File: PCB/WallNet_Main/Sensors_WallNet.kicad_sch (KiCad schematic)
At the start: 28 parts, among them J201 Conn_01x04_Pin, J202 Conn_01x07_Socket, J203 Conn_02x12_Counter_Clockwise, Q2 BSS138, SW2 SW, U201 CPT-9019B-SMT-TR, U202 SAM-M10Q-00B

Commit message: Schematic done, updated layout
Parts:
- C201, C202, C203, C204, C205, C206, C207, C208, C209, C210, C211, C212: footprint Capacitor_SMD:C_0201_0603Metric -> Capacitor_SMD:C_0603_1608Metric
- J201: footprint Connector_Molex:Molex_CLIK-Mate_502494-0470_1x04-1MP_P2.00mm_Horizontal -> Connector_Molex:Molex_PicoBlade_53261-0471_1x04-1MP_P1.25mm_Horizontal
- R201, R202, R203, R204, R205: footprint Resistor_SMD:R_0201_0603Metric -> Resistor_SMD:R_0603_1608Metric
- renumbered D1 to D201, D2 to D202, D3 to D203, Q2 to Q201, SW2 to SW201
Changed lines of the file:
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@@
 			)
 		)
-		(property "Footprint" "Resistor_SMD:R_0201_0603Metric"
+		(property "Footprint" "Resistor_SMD:R_0603_1608Metric"
 			(at 127 149.86 0)
 			(effects
@@
 			)
 		)
-		(property "Footprint" "Capacitor_SMD:C_0201_0603Metric"
+		(property "Footprint" "Capacitor_SMD:C_0603_1608Metric"
 			(at 241.3 90.17 0)
 			(effects
@@
 			)
 		)
-		(property "Footprint" "Capacitor_SMD:C_0201_0603Metric"
+		(property "Footprint" "Capacitor_SMD:C_0603_1608Metric"
 			(at 190.5 90.17 0)
 			(effects
@@
 			)
 		)
-		(property "Footprint" "Capacitor_SMD:C_0201_0603Metric"
+		(property "Footprint" "Capacitor_SMD:C_0603_1608Metric"
 			(at 231.14 90.17 0)
 			(effects
@@
 			)
 		)
-		(property "Footprint" "Capacitor_SMD:C_0201_0603Metric"
+		(property "Footprint" "Capacitor_SMD:C_0603_1608Metric"
 			(at 261.62 54.61 0)
 			(effects
@@
 			)
 		)
-		(property "Footprint" "Capacitor_SMD:C_0201_0603Metric"
+		(property "Footprint" "Capacitor_SMD:C_0603_1608Metric"
 			(at 200.66 90.17 0)
 			(effects
@@
 			)
 		)
-		(property "Footprint" "Capacitor_SMD:C_0201_0603Metric"
+		(property "Footprint" "Capacitor_SMD:C_0603_1608Metric"
 			(at 45.72 100.33 0)
 			(effects
@@
 			)
 		)
-		(property "Footprint" "Capacitor_SMD:C_0201_0603Metric"
+		(property "Footprint" "Capacitor_SMD:C_0603_1608Metric"
 			(at 250.19 90.17 0)
 			(effects
@@
 			)
 		)
-		(property "Footprint" "Capacitor_SMD:C_0201_0603Metric"
+		(property "Footprint" "Capacitor_SMD:C_0603_1608Metric"
 			(at 270.51 90.17 0)
 			(effects
@@
 			)
 		)
-		(property "Footprint" "Connector_Molex:Molex_CLIK-Mate_502494-0470_1x04-1MP_P2.00mm_Horizontal"
+		(property "Footprint" "Connector_Molex:Molex_PicoBlade_53261-0471_1x04-1MP_P1.25mm_Horizontal"
 			(at 53.34 124.46 0)
 			(effects
@@
 		(on_board yes)
 		(dnp no)
-		(property "Reference" "D3"
+		(property "Reference" "D203"
 			(at 248.92 63.8174 90)
 			(effects
@@
 			(project "WallNet_Main"
 				(path "/3272dd14-9e34-4275-b10b-c06dab1b3ca1/14f35c0a-7540-4617-95f9-116bbddd487f"
-					(reference "D3")
+					(reference "D203")
 					(unit 1)
 				)
@@
 		(on_board yes)
 		(dnp no)
-		(property "Reference" "Q2"
+		(property "Reference" "Q201"
 			(at 270.51 34.2899 0)
 			(effects
@@
 			(project ""
 				(path "/3272dd14-9e34-4275-b10b-c06dab1b3ca1/14f35c0a-7540-4617-95f9-116bbddd487f"
-					(reference "Q2")
+					(reference "Q201")
 					(unit 1)
 				)
@@
 		(on_board yes)
 		(dnp no)
-		(property "Reference" "D2"
+		(property "Reference" "D202"
 			(at 259.08 63.8174 90)
 			(effects
@@
 			(project "WallNet_Main"
 				(path "/3272dd14-9e34-4275-b10b-c06dab1b3ca1/14f35c0a-7540-4617-95f9-116bbddd487f"
-					(reference "D2")
+					(reference "D202")
 					(unit 1)
 				)
@@
 			)
 		)
-		(property "Footprint" "Resistor_SMD:R_0201_0603Metric"
+		(property "Footprint" "Resistor_SMD:R_0603_1608Metric"
 			(at 133.35 152.4 0)
 			(effects
@@
 			)
 		)
-		(property "Footprint" "Capacitor_SMD:C_0201_0603Metric"
+		(property "Footprint" "Capacitor_SMD:C_0603_1608Metric"
 			(at 260.35 90.17 0)
 			(effects
@@
 			)
 		)
-		(property "Footprint" "Capacitor_SMD:C_0201_0603Metric"
+		(property "Footprint" "Capacitor_SMD:C_0603_1608Metric"
 			(at 210.82 90.17 0)
 			(effects
@@
 			)
 		)
-		(property "Footprint" "Capacitor_SMD:C_0201_0603Metric"
+		(property "Footprint" "Capacitor_SMD:C_0603_1608Metric"
 			(at 248.92 45.72 0)
 			(effects
@@
 		(on_board yes)
 		(dnp no)
-		(property "Reference" "SW2"
+		(property "Reference" "SW201"
 			(at 59.436 95.25 0)
 			(effects
@@
 			(project "WallNet_Main"
 				(path "/3272dd14-9e34-4275-b10b-c06dab1b3ca1/14f35c0a-7540-4617-95f9-116bbddd487f"
-					(reference "SW2")
+					(reference "SW201")
 					(unit 1)
 				)
@@
 			)
 		)
-		(property "Footprint" "Resistor_SMD:R_0201_0603Metric"
+		(property "Footprint" "Resistor_SMD:R_0603_1608Metric"
 			(at 251.46 35.56 0)
 			(effects
@@
 			)
 		)
-		(property "Footprint" "Capacitor_SMD:C_0201_0603Metric"
+		(property "Footprint" "Capacitor_SMD:C_0603_1608Metric"
 			(at 220.98 90.17 0)
 			(effects
@@
 		(on_board yes)
 		(dnp no)
-		(property "Reference" "D1"
+		(property "Reference" "D201"
 			(at 269.24 63.8174 90)
 			(effects
@@
 			(project ""
 				(path "/3272dd14-9e34-4275-b10b-c06dab1b3ca1/14f35c0a-7540-4617-95f9-116bbddd487f"
-					(reference "D1")
+					(reference "D201")
 					(unit 1)
 				)
@@
 			)
 		)
-		(property "Footprint" "Resistor_SMD:R_0201_0603Metric"
+		(property "Footprint" "Resistor_SMD:R_0603_1608Metric"
 			(at 251.46 25.4 0)
 			(effects
@@
 			)
 		)
-		(property "Footprint" "Resistor_SMD:R_0201_0603Metric"
+		(property "Footprint" "Resistor_SMD:R_0603_1608Metric"
 			(at 40.64 95.25 0)
 			(effects

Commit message: Manager Meeting Updates
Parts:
- SW201: footprint (none) -> 436331045822:4363X10458XX
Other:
- note added: "Implement Backup circuit (Socket connector)"
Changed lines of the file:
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@@
 		)
 	)
+	(text "Implement Backup circuit (Socket connector)"
+		(exclude_from_sim no)
+		(at 230.886 106.172 0)
+		(effects
+			(font
+				(size 1.27 1.27)
+			)
+		)
+	)
 	(text "Buzzer"
 		(exclude_from_sim no)
@@
 			)
 		)
-		(property "Footprint" ""
+		(property "Footprint" "436331045822:4363X10458XX"
 			(at 52.07 97.79 0)
 			(effects

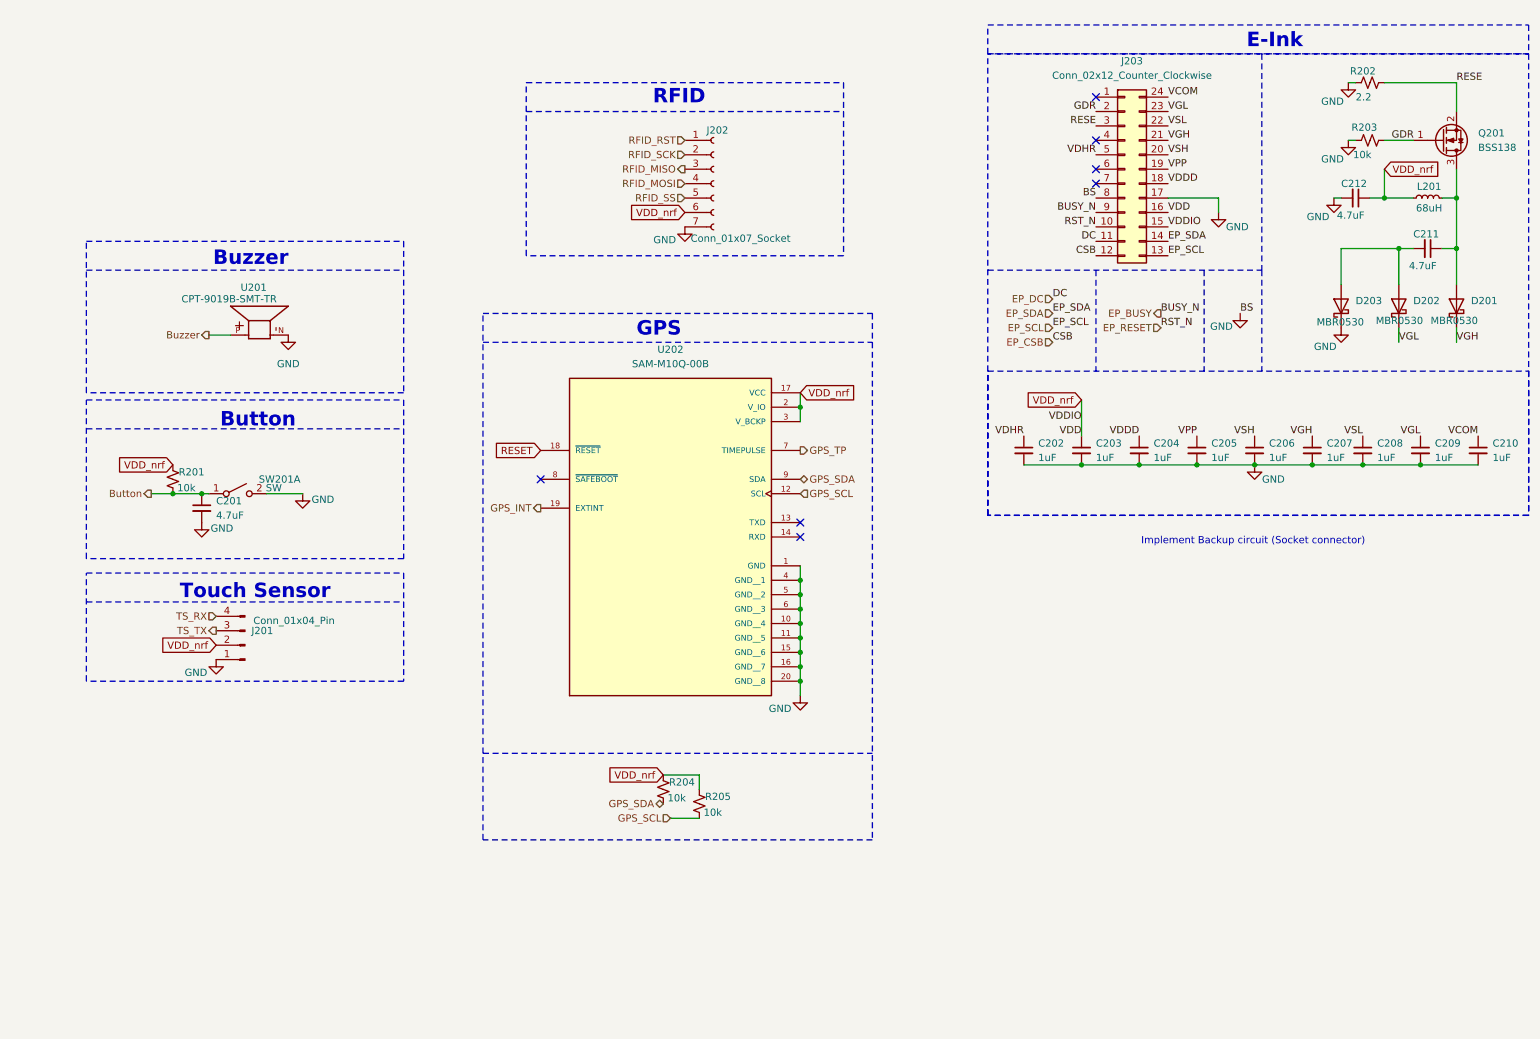
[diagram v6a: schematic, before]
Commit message: "added test point debugging and mounting holes"
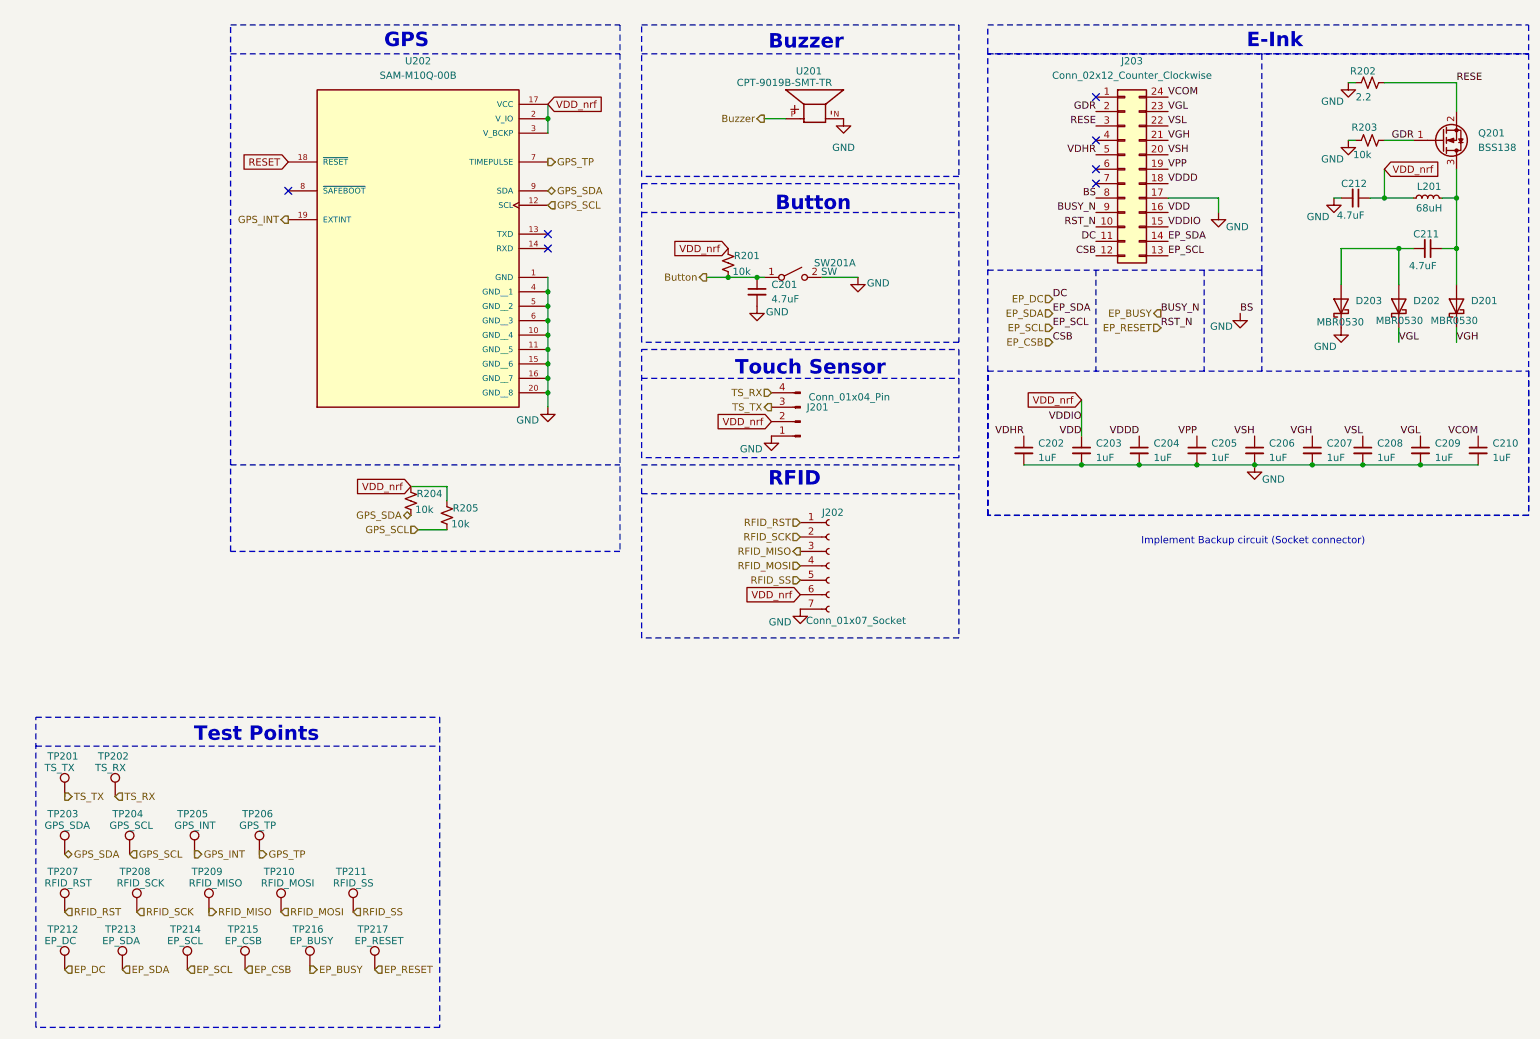
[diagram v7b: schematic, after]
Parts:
- added TP201: TS_TX, 5001:KEYSTONE_5001, symbol Connector:TestPoint
- added TP202: TS_RX, 5001:KEYSTONE_5001, symbol Connector:TestPoint
- added TP203: GPS_SDA, 5001:KEYSTONE_5001, symbol Connector:TestPoint
- added TP204: GPS_SCL, 5001:KEYSTONE_5001, symbol Connector:TestPoint
- added TP205: GPS_INT, 5001:KEYSTONE_5001, symbol Connector:TestPoint
- added TP206: GPS_TP, 5001:KEYSTONE_5001, symbol Connector:TestPoint
- added TP207: RFID_RST, 5001:KEYSTONE_5001, symbol Connector:TestPoint
- added TP208: RFID_SCK, 5001:KEYSTONE_5001, symbol Connector:TestPoint
- added TP209: RFID_MISO, 5001:KEYSTONE_5001, symbol Connector:TestPoint
- added TP210: RFID_MOSI, 5001:KEYSTONE_5001, symbol Connector:TestPoint
- added TP211: RFID_SS, 5001:KEYSTONE_5001, symbol Connector:TestPoint
- added TP212: EP_DC, 5001:KEYSTONE_5001, symbol Connector:TestPoint
- added TP213: EP_SDA, 5001:KEYSTONE_5001, symbol Connector:TestPoint
- added TP214: EP_SCL, 5001:KEYSTONE_5001, symbol Connector:TestPoint
- added TP215: EP_CSB, 5001:KEYSTONE_5001, symbol Connector:TestPoint
- added TP216: EP_BUSY, 5001:KEYSTONE_5001, symbol Connector:TestPoint
- added TP217: EP_RESET, 5001:KEYSTONE_5001, symbol Connector:TestPoint
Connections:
- net EP_BUSY: now also TP216.1
- net EP_CSB: now also TP215.1
- net EP_DC: now also TP212.1
- net EP_RESET: now also TP217.1
- net EP_SCL: now also TP214.1
- net EP_SDA: now also TP213.1
- net GPS_INT: now also TP205.1
- net GPS_SCL: now also TP204.1
- net GPS_SDA: now also TP203.1
- net GPS_TP: now also TP206.1
- net RFID_MISO: now also TP209.1
- net RFID_MOSI: now also TP210.1
- net RFID_RST: now also TP207.1
- net RFID_SCK: now also TP208.1
- net RFID_SS: now also TP211.1
- net TS_RX: now also TP202.1
- net TS_TX: now also TP201.1
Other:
- note added: "Test Points"
- moved on the sheet: C201, J201, J202, R201, R204, R205, SW201A, U201, U202

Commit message: Updated, Schematic done, waiting on Layout
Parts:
- removed SW201: SW, 436331045822:4363X10458XX, symbol Switch:SW_DPST_x2
- added S201: 436331045822, 436331045822:4363X10458XX, symbol 436331045822:436331045822
- L201: footprint (none) -> VLS3015CX_680M_H:IND_VLS3015CX-680M-H
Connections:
- net Button: now also S201.1, S201.3
- net GND: now also S201.2, S201.4
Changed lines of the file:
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@@
 	)
 	(junction
+		(at 153.67 59.69)
+		(diameter 0)
+		(color 0 0 0 0)
+	)
+	(junction
 		(at 266.7 45.72)
 		(diameter 0)
@@
 		(at 106.68 52.07)
 	)
+	(wire
+		(pts
+			(xy 153.67 59.69) (xy 161.29 59.69)
+		)
+		(stroke
+			(width 0)
+			(type default)
+		)
+	)
 	(polyline
 		(pts
@@
 	(wire
 		(pts
+			(xy 152.4 49.53) (xy 153.67 49.53)
+		)
+		(stroke
+			(width 0)
+			(type default)
+		)
+	)
+	(wire
+		(pts
 			(xy 247.65 25.4) (xy 248.92 25.4)
 		)
@@
 	(wire
 		(pts
+			(xy 144.78 49.53) (xy 143.51 49.53)
+		)
+		(stroke
+			(width 0)
+			(type default)
+		)
+	)
+	(wire
+		(pts
 			(xy 256.54 68.58) (xy 256.54 71.12)
 		)
@@
 	(wire
 		(pts
+			(xy 143.51 49.53) (xy 143.51 59.69)
+		)
+		(stroke
+			(width 0)
+			(type default)
+		)
+	)
+	(wire
+		(pts
 			(xy 190.5 92.71) (xy 200.66 92.71)
 		)
@@
 	(wire
 		(pts
-			(xy 161.29 59.69) (xy 154.94 59.69)
+			(xy 254 45.72) (xy 259.08 45.72)
 		)
 		(stroke
@@
 	(wire
 		(pts
-			(xy 254 45.72) (xy 259.08 45.72)
+			(xy 246.38 54.61) (xy 256.54 54.61)
 		)
 		(stroke
@@
 	(wire
 		(pts
-			(xy 246.38 54.61) (xy 256.54 54.61)
+			(xy 152.4 59.69) (xy 153.67 59.69)
 		)
 		(stroke
@@
 	(wire
 		(pts
+			(xy 153.67 49.53) (xy 153.67 59.69)
+		)
+		(stroke
+			(width 0)
+			(type default)
+		)
+	)
+	(wire
+		(pts
 			(xy 266.7 25.4) (xy 266.7 30.48)
 		)
@@
 	)
 	(symbol
+		(lib_id "436331045822:436331045822")
+		(at 149.86 54.61 90)
+		(unit 1)
+		(exclude_from_sim no)
+		(in_bom yes)
+		(on_board yes)
+		(dnp no)
+		(fields_autoplaced yes)
+		(property "Reference" "S201"
+			(at 153.67 53.3399 90)
+			(effects
+				(font
+					(size 1.27 1.27)
+				)
+				(justify right)
+			)
+		)
+		(property "Value" "436331045822"
+			(at 153.67 55.8799 90)
+			(effects
+				(font
+					(size 1.27 1.27)
+				)
+				(justify right)
+			)
+		)
+		(property "Footprint" "436331045822:4363X10458XX"
+			(at 149.86 54.61 0)
+			(effects
+				(font
+					(size 1.27 1.27)
+				)
+				(justify bottom)
+				(hide yes)
+			)
+		)
+		(property "Datasheet" ""
+			(at 149.86 54.61 0)
+			(effects
+				(font
+					(size 1.27 1.27)
+				)
+				(hide yes)
+			)
+		)
+		(property "Description" ""
+			(at 149.86 54.61 0)
+			(effects
+				(font
+					(size 1.27 1.27)
+				)
+				(hide yes)
+			)
+		)
+		(pin "3"
+		)
+		(pin "2"
+		)
+		(pin "4"
+		)
+		(pin "1"
+		)
+		(instances
+			(project ""
+				(path "/3272dd14-9e34-4275-b10b-c06dab1b3ca1/14f35c0a-7540-4617-95f9-116bbddd487f"
+					(reference "S201")
+					(unit 1)
+				)
+			)
+		)
+	)
+	(symbol
 		(lib_id "Connector:TestPoint")
 		(at 21.59 181.61 0)
@@
 	)
 	(symbol
-		(lib_id "Switch:SW_DPST_x2")
-		(at 149.86 59.69 0)
-		(unit 1)
-		(exclude_from_sim no)
-		(in_bom yes)
-		(on_board yes)
-		(dnp no)
-		(property "Reference" "SW201"
-			(at 157.226 57.15 0)
-			(effects
-				(font
-					(size 1.27 1.27)
-				)
-			)
-		)
-		(property "Value" "SW"
-			(at 156.21 58.674 0)
-			(effects
-				(font
-					(size 1.27 1.27)
-				)
-			)
-		)
-		(property "Footprint" "436331045822:4363X10458XX"
-			(at 149.86 59.69 0)
-			(effects
-				(font
-					(size 1.27 1.27)
-				)
-				(hide yes)
-			)
-		)
-		(property "Datasheet" "~"
-			(at 149.86 59.69 0)
-			(effects
-				(font
-					(size 1.27 1.27)
-				)
-				(hide yes)
-			)
-		)
-		(property "Description" "Single Pole Single Throw (SPST) switch, separate symbol"
-			(at 149.86 59.69 0)
-			(effects
-				(font
-					(size 1.27 1.27)
-				)
-				(hide yes)
-			)
-		)
-		(pin "2"
-		)
-		(pin "3"
-		)
-		(pin "1"
-		)
-		(pin "4"
-		)
-		(instances
-			(project "WallNet_Main"
-				(path "/3272dd14-9e34-4275-b10b-c06dab1b3ca1/14f35c0a-7540-4617-95f9-116bbddd487f"
-					(reference "SW201")
-					(unit 1)
-				)
-			)
-		)
-	)
-	(symbol
 		(lib_id "CPT-9019B-SMT-TR:CPT-9019B-SMT-TR")
 		(at 153.67 29.21 90)
@@
 			)
 		)
-		(property "Footprint" ""
+		(property "Footprint" "VLS3015CX_680M_H:IND_VLS3015CX-680M-H"
 			(at 261.62 45.72 0)
 			(effects
